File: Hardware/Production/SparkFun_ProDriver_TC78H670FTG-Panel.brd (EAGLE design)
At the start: 50.8 x 57.1 mm, 137 parts, among them J2 LATCH, J3 PTH, J4 LATCH, J5 LATCH, J6 PTH, J7 LATCH, J8 PTH, U1 TC78H670FTG, U2 LM1117

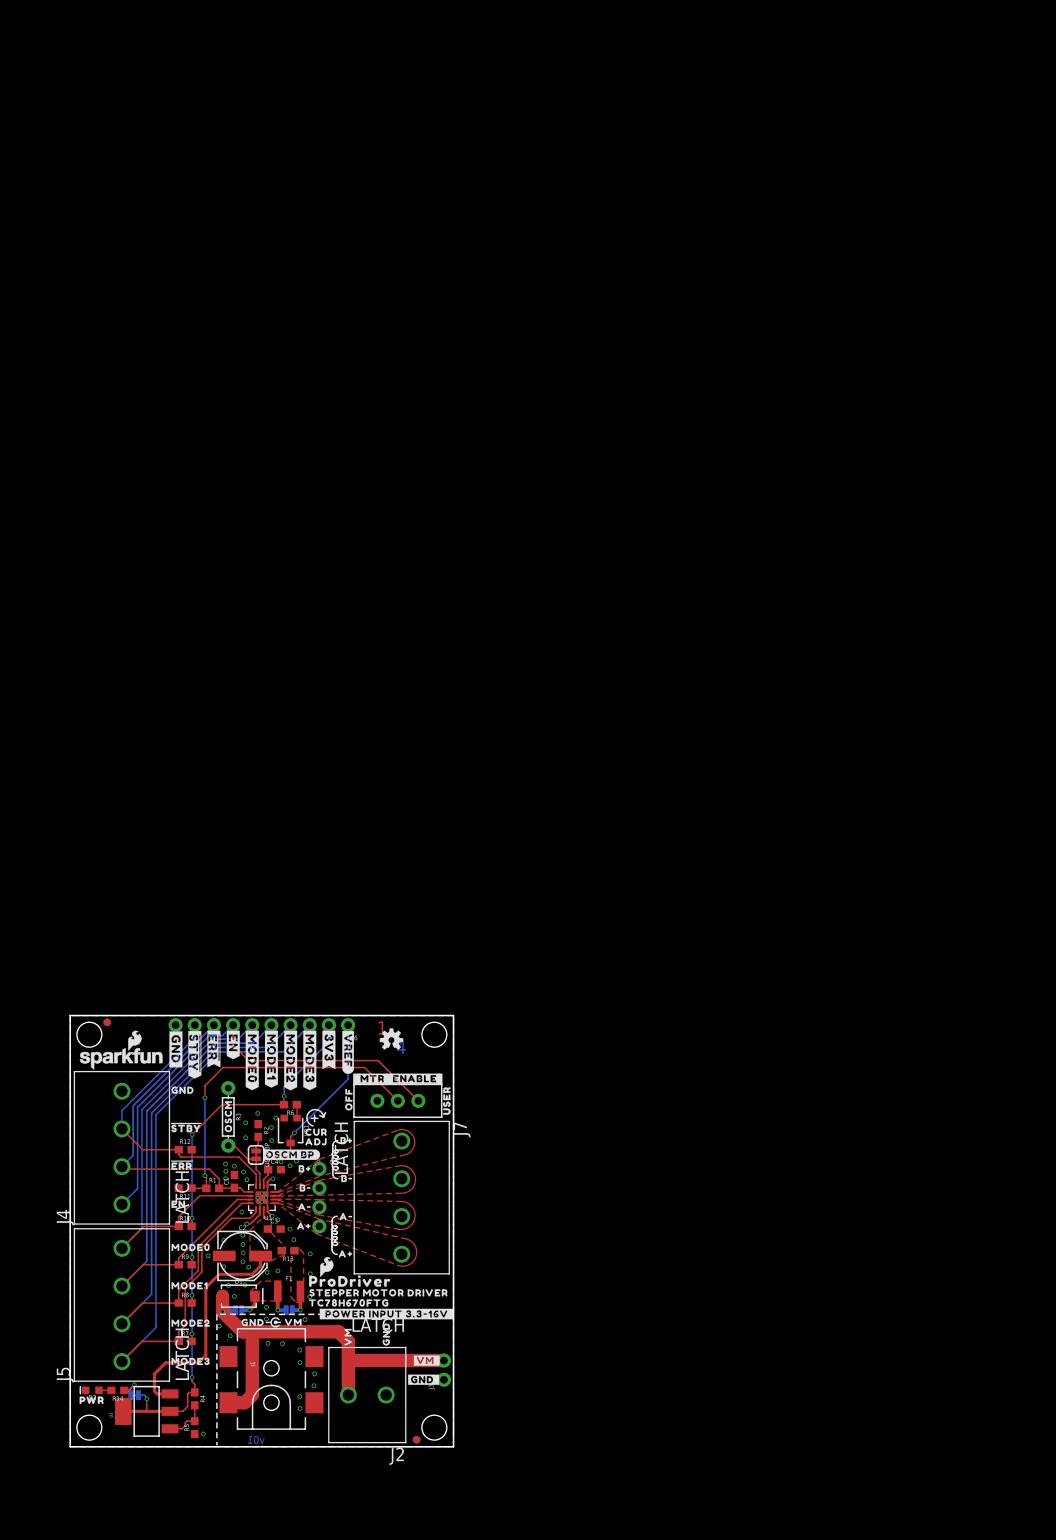
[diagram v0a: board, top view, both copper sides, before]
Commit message: production files - also decided to go with 1 OZ copper
-panelized for proto panel order 2x2
-removed "2OZ Copper" note from special ordering instructions. Fab house for protos (JLC) has huge price jump for 2 OZ, so gonna try 1 OZ for protos and see how heat sinking does.
-adjusted ordering instrutions text file to reflext black soldermask
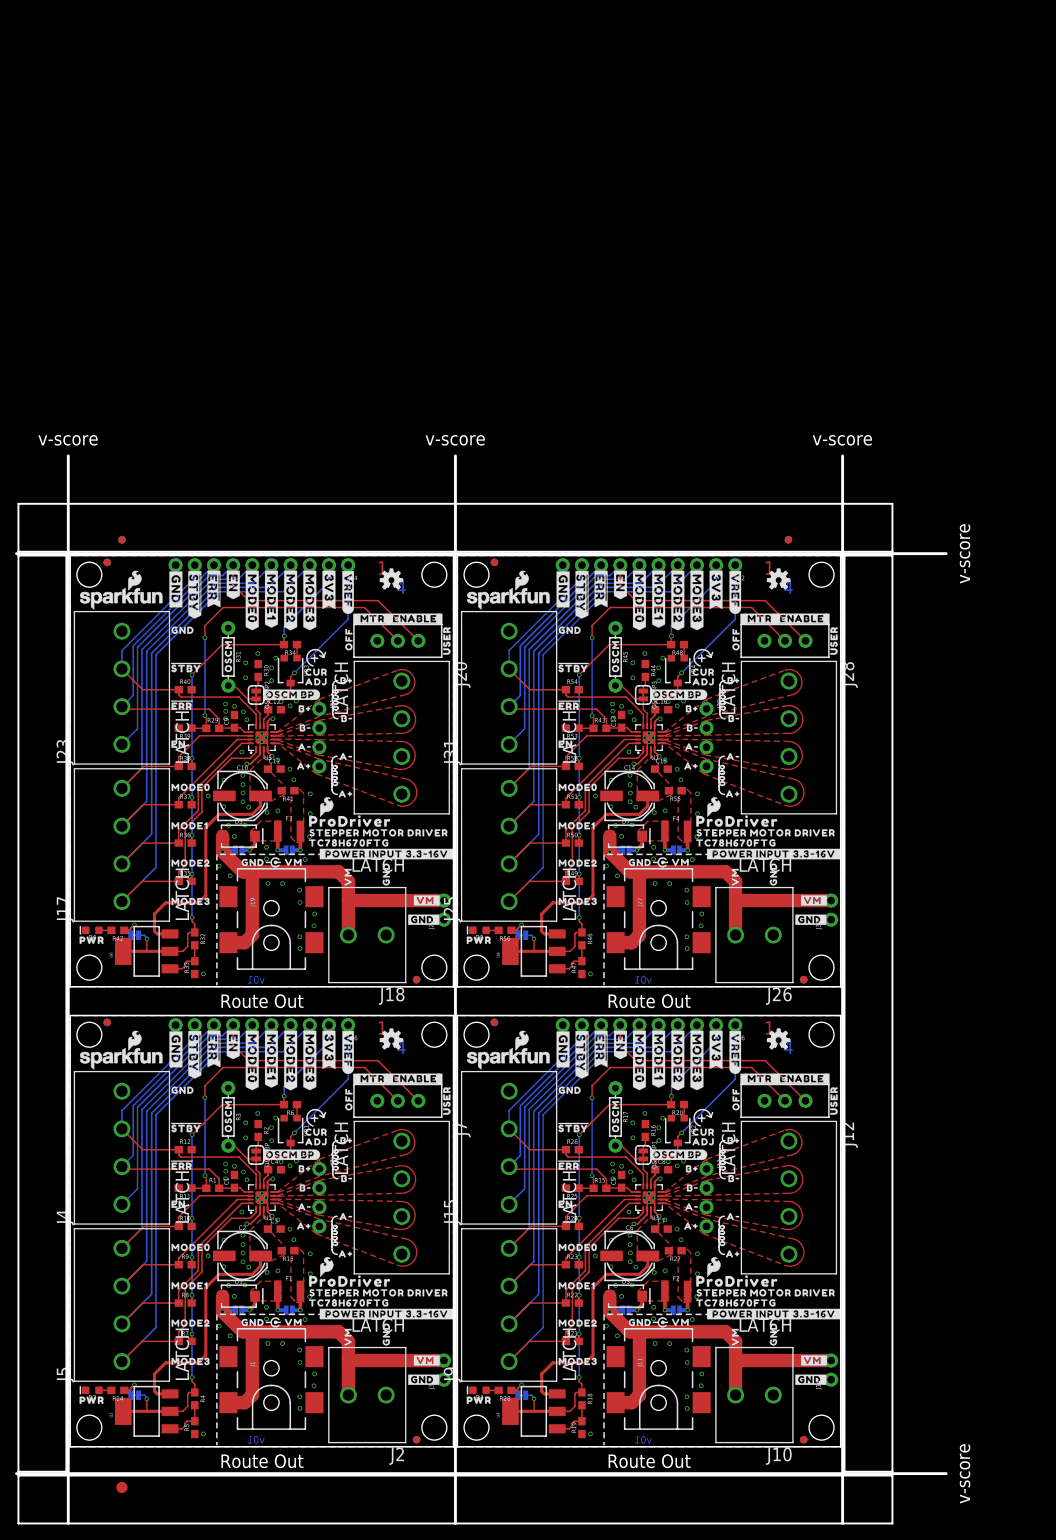
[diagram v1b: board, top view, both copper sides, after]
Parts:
- removed FRAME1: FRAME-LETTER, SparkFun-Aesthetics:CREATIVE_COMMONS
- added C10, C14, C6: 47uF, SparkFun-Capacitors:PANASONIC_D
- added C11, C12, C15, C16, C7, C8: 0.1uF, SparkFun-Capacitors:0603
- added C13, C5, C9: 22nF, SparkFun-Capacitors:0603
- added D1BP1, D1BP2, D1BP3, PTCBP1, PTCBP2, PTCBP3: (no value), SparkFun-Jumpers:SMT-JUMPER_2_NO_SILK
- added D3, D5, D7: 3A/40V/500mV, SparkFun-DiscreteSemi:SMA-DIODE
- added D4, D6, D8: RED, SparkFun-LED:LED-0603
- added E$1, E$2, E$3, E$4: (no value), SparkFun-Aesthetics:FIDUCIAL-1X2
- added E$5: (no value), SparkFun-Retired:FIDUCIAL-1.5X3
- added F2, F3, F4: 16V/1.1A(2.2A TRIP), TC78H670FTG:1210
- added FID10, FID11, FID12, FID13, FID14, FID15, FID16, FID5, FID6, FID7, FID8, FID9: FIDUCIAL1X2, SparkFun-Aesthetics:FIDUCIAL-1X2
- added J10, J18, J26: LATCH, SparkFun-Connectors:LATCHTERMINAL-5MM-2
- added J11, J19, J27: (no value), SparkFun-Connectors:POWER_JACK_SMD_OVERPASTE_TOE
- added J12, J15, J17, J20, J23, J25, J28, J31, J9: LATCH, SparkFun-Connectors:LATCHTERMINAL-5MM-4
- added J13, J21, J29: PTH, SparkFun-Connectors:1X04_NO_SILK
- added J14, J22, J30: PTH, SparkFun-Connectors:1X02_NO_SILK
- added J16, J24, J32: PTH, SparkFun-Connectors:1X10_NO_SILK
- added JP1, JP2, JP3: LED, SparkFun-Jumpers:SMT-JUMPER_2_NC_TRACE_SILK
- added LOGO10, LOGO14, LOGO4: OSHW-LOGOS, SparkFun-Aesthetics:OSHW-LOGO-S
- added LOGO11, LOGO13, LOGO15, LOGO7, LOGO9: SFE_LOGO_NAME_FLAME.1_INCH, SparkFun-Aesthetics:SFE_LOGO_NAME_FLAME_.1
- added LOGO12, LOGO16, LOGO8: SFE_LOGO_FLAME.1_INCH, SparkFun-Aesthetics:SFE_LOGO_FLAME_.1
- added OSCMBP1, OSCMBP2, OSCMBP3: (no value), SparkFun-Jumpers:SMT-JUMPER_2_NC_TRACE_SILK
- added R15, R29, R43: 10k, SparkFun-Resistors:0603
- added R16, R30, R44: 47k, SparkFun-Resistors:0603
- added R17, R31, R45: DNP, SparkFun-Resistors:AXIAL-0.3
- added R18, R32, R46: 240, SparkFun-Resistors:0603
- added R19, R33, R47: 390, SparkFun-Resistors:0603
- added R20, R34, R48: 8.2k, SparkFun-Resistors:0603
- added R21, R22, R23, R24, R25, R26, R35, R36, R37, R38, R39, R40, R49, R50, R51, R52, R53, R54: 22k, SparkFun-Resistors:0603
- added R27, R41, R55: 0, SparkFun-Resistors:0603
- added R28, R42, R56: 1k, SparkFun-Resistors:0603
- added S2, S3, S4: (no value), SparkFun-Switches:SWITCH_SPDT_PTH_11.6X4.0MM_LOCK
- added STANDOFF10, STANDOFF11, STANDOFF12, STANDOFF13, STANDOFF14, STANDOFF15, STANDOFF16, STANDOFF5, STANDOFF6, STANDOFF7, STANDOFF8, STANDOFF9: STAND-OFF, SparkFun-Electromechanical:STAND-OFF
- added U$100, U$186, U$272: (no value), output:MODE10
- added U$101, U$187, U$273: (no value), output:MODE20
- added U$102, U$188, U$274: (no value), output:MODE00
- added U$103, U$189, U$275: (no value), output:#GND_#0
- added U$104, U$190, U$276: (no value), output:#VM_#0
- added U$105, U$177, U$179, U$191, U$263, U$265, U$277, U$91, U$93: (no value), output:GND6
- added U$106, U$178, U$192, U$264, U$278, U$92: (no value), output:VM10
- added U$107, U$159, U$193, U$245, U$279, U$331: (no value), output:TC78H670FTG0
- added U$108, U$160, U$194, U$246, U$280, U$332: (no value), output:STEPPER_MOTOR_DRIVER0
- added U$109, U$144, U$147, U$195, U$230, U$233, U$281, U$316, U$319: (no value), output:#GND#0
- added U$110, U$161, U$196, U$247, U$282, U$333: (no value), output:PRODRIVER0
- added U$111, U$197, U$283: (no value), output:#MTR#0
- added U$112, U$198, U$284: (no value), output:#ENABLE#0
- added U$113, U$174, U$199, U$260, U$285, U$71: (no value), output:B#1
- added U$114, U$173, U$200, U$259, U$286, U$41: (no value), output:B#0
- added U$115, U$176, U$201, U$262, U$287, U$90: (no value), output:A#3
- added U$116, U$175, U$202, U$261, U$288, U$74: (no value), output:A#2
- added U$117, U$203, U$289: (no value), output:EN0
- added U$118, U$204, U$290: (no value), output:#EN#2
- added U$119, U$149, U$205, U$235, U$291, U$321: (no value), output:#MODE0#4
- added U$120, U$150, U$206, U$236, U$292, U$322: (no value), output:#MODE1#4
- added U$121, U$151, U$207, U$237, U$293, U$323: (no value), output:#MODE2#4
- added U$122, U$152, U$208, U$238, U$294, U$324: (no value), output:#MODE3#4
- added U$123, U$153, U$209, U$239, U$295, U$325: (no value), output:#3V3#4
- added U$124, U$154, U$210, U$240, U$296, U$326: (no value), output:#VREF#0
- added U$125, U$211, U$297: (no value), output:#D1_BP#0
- added U$126, U$132, U$212, U$218, U$298, U$304: (no value), output:#B##0
- added U$127, U$133, U$213, U$219, U$299, U$305: (no value), output:#B##1
- added U$128, U$134, U$214, U$220, U$300, U$306: (no value), output:#A##2
- added U$129, U$135, U$215, U$221, U$301, U$307: (no value), output:#A##3
- added U$130, U$145, U$216, U$231, U$302, U$317: (no value), output:#GND#5
- added U$131, U$217, U$303: (no value), output:#_EN_#0
- added U$136, U$222, U$308: (no value), output:#MODE0#0
- added U$137, U$223, U$309: (no value), output:#MODE1#0
- added U$138, U$224, U$310: (no value), output:#MODE2#0
- added U$139, U$225, U$311: (no value), output:#MODE3#0
- added U$140, U$226, U$312: (no value), output:#CLK#S_CLK#0
- added U$141, U$227, U$313: (no value), output:#SET_EN#LATCH#0
- added U$142, U$228, U$314: (no value), output:#UP#DW#S_DATA#0
- added U$143, U$146, U$229, U$232, U$315, U$318: (no value), output:#VM#0
- added U$148, U$234, U$320: (no value), output:#EN#4
- added U$155, U$241, U$327: (no value), output:#CW#CCW#0
- added U$156, U$242, U$328: (no value), output:#PTC_BP#0
- added U$157, U$243, U$329: (no value), output:#LED#0
- added U$158, U$244, U$330: (no value), output:PWR0
- added U$162, U$248, U$334: (no value), output:##STBY##0
- added U$163, U$164, U$249, U$250, U$335, U$336: (no value), output:##STBY##1
- added U$165, U$251, U$337: (no value), output:#STBY#2
- added U$166, U$252, U$338: (no value), output:#ERR#3
- added U$167, U$253, U$339: (no value), output:##ERR##5
- added U$168, U$169, U$254, U$255, U$340, U$341: (no value), output:##ERR##6
- added U$170, U$256, U$342: (no value), output:USER0
- added U$171, U$257, U$343: (no value), output:#OSCM_BP#0
- added U$172, U$258, U$344: (no value), output:#_POWER_INPUT_3#3#16V_#0
- added U$180, U$266, U$94: (no value), output:OFF0
- added U$181, U$267, U$95: (no value), output:OSCM0
- added U$182, U$268, U$96: (no value), output:CUR0
- added U$183, U$269, U$97: (no value), output:ADJ0
- added U$184, U$270, U$98: (no value), TC78H670FTG:CURRENT_ADJUST
- added U$185, U$271, U$99: (no value), output:MODE30
- added U3, U5, U7: TC78H670FTG, TC78H670FTG:P-VQFN16-0303-0.50-001
- added U4, U6, U8: LM1117, SparkFun-IC-Power:SOT223
- added VR2, VR3, VR4: 10k, SparkFun-Resistors:TRIMPOT-SMD-3MM-CLOSED
- LOGO3: value SPECIAL_INSTRUCTIONS-ORDERING -> SFE_LOGO_NAME_FLAME.1_INCH; device SparkFun-Aesthetics:ORDERING_INSTRUCTIONS -> SparkFun-Aesthetics:SFE_LOGO_NAME_FLAME_.1
- moved LOGO3 106.6 mm to (58.1, 51.4)
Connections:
- new net !ERR1: C5.1, J15.2, J16.8, R15.2, U3.13
- new net !ERR2: C9.1, J23.2, J24.8, R29.2, U5.13
- new net !ERR3: C13.1, J31.2, J32.8, R43.2, U7.13
- new net !STBY1: J15.3, J16.9, R26.1, U3.12
- new net !STBY2: J23.3, J24.9, R40.1, U5.12
- new net !STBY3: J31.3, J32.9, R54.1, U7.12
- new net 3.3V1: J16.2, JP1.2, R18.1, R20.2, R21.2, R22.2, R23.2, R24.2, U4.2, U4.4
- new net 3.3V2: J24.2, JP2.2, R32.1, R34.2, R35.2, R36.2, R37.2, R38.2, U6.2, U6.4
- new net 3.3V3: J32.2, JP3.2, R46.1, R48.2, R49.2, R50.2, R51.2, R52.2, U8.2, U8.4
- new net EN1: J15.1, J16.7, S2.1
- new net EN2: J23.1, J24.7, S3.1
- new net EN3: J31.1, J32.7, S4.1
- new net GND1: C5.2, C6.-, C7.2, C8.2, D4.C, J10.1, J11.GND, J11.P$4, J14.1, J15.4, J16.10, R16.1, R17.P$1, R19.1, R25.2, R26.2, U3.17, U3.2, U3.4, U3.9, VR2.3
- new net GND2: C10.-, C11.2, C12.2, C9.2, D6.C, J18.1, J19.GND, J19.P$4, J22.1, J23.4, J24.10, R30.1, R31.P$1, R33.1, R39.2, R40.2, U5.17, U5.2, U5.4, U5.9, VR3.3
- new net GND3: C13.2, C14.-, C15.2, C16.2, D8.C, J26.1, J27.GND, J27.P$4, J30.1, J31.4, J32.10, R44.1, R45.P$1, R47.1, R53.2, R54.2, U7.17, U7.2, U7.4, U7.9, VR4.3
- new net MODE10: J17.3, J24.5, R37.1, U5.15
- new net MODE11: J17.4, J24.6, R38.1, U5.14
- new net MODE12: J25.1, J32.3, R49.1, U7.1
- new net MODE13: J25.2, J32.4, R50.1, U7.16
- new net MODE14: J25.3, J32.5, R51.1, U7.15
- new net MODE15: J25.4, J32.6, R52.1, U7.14
- new net MODE4: J16.3, J9.1, R21.1, U3.1
- new net MODE5: J16.4, J9.2, R22.1, U3.16
- new net MODE6: J16.5, J9.3, R23.1, U3.15
- new net MODE7: J16.6, J9.4, R24.1, U3.14
- new net MODE8: J17.1, J24.3, R35.1, U5.1
- new net MODE9: J17.2, J24.4, R36.1, U5.16
- new net N$10: OSCMBP1.1, R16.2
- new net N$11: R18.2, R19.2, U4.1
- new net N$13: R20.1, VR2.1
- new net N$14: D1BP1.2, D3.C, F2.1, PTCBP1.1
- new net N$15: F2.2, PTCBP1.2, R27.1
- new net N$16: D4.A, R28.2
- new net N$17: JP1.1, R28.1
- new net N$18: R15.1, R25.1, S2.2
- new net N$21: OSCMBP2.1, R30.2
- new net N$22: R32.2, R33.2, U6.1
- new net N$23: R34.1, VR3.1
- new net N$24: D1BP2.2, D5.C, F3.1, PTCBP2.1
- new net N$25: F3.2, PTCBP2.2, R41.1
- new net N$26: D6.A, R42.2
- new net N$27: JP2.1, R42.1
- new net N$28: R29.1, R39.1, S3.2
- new net N$31: OSCMBP3.1, R44.2
- new net N$32: R46.2, R47.2, U8.1
- new net N$33: R48.1, VR4.1
- new net N$34: D1BP3.2, D7.C, F4.1, PTCBP3.1
- new net N$35: F4.2, PTCBP3.2, R55.1
- new net N$36: D8.A, R56.2
- new net N$37: JP3.1, R56.1
- new net N$38: R43.1, R53.1, S4.2
- new net OSCM1: OSCMBP1.2, R17.P$2, U3.11
- new net OSCM2: OSCMBP2.2, R31.P$2, U5.11
- new net OSCM3: OSCMBP3.2, R45.P$2, U7.11
- new net OUT_A+1: J12.4, J13.4, U3.5
- new net OUT_A+2: J20.4, J21.4, U5.5
- new net OUT_A+3: J28.4, J29.4, U7.5
- new net OUT_A-1: J12.3, J13.3, U3.6
- new net OUT_A-2: J20.3, J21.3, U5.6
- new net OUT_A-3: J28.3, J29.3, U7.6
- new net OUT_B+1: J12.1, J13.1, U3.8
- new net OUT_B+2: J20.1, J21.1, U5.8
- new net OUT_B+3: J28.1, J29.1, U7.8
- new net OUT_B-1: J12.2, J13.2, U3.7
- new net OUT_B-2: J20.2, J21.2, U5.7
- new net OUT_B-3: J28.2, J29.2, U7.7
- new net RAW1: D1BP1.1, D3.A, J10.2, J11.VIN0, J14.2
- new net RAW2: D1BP2.1, D5.A, J18.2, J19.VIN0, J22.2
- new net RAW3: D1BP3.1, D7.A, J26.2, J27.VIN0, J30.2
- new net VM1: C6.+, C7.1, R27.2, U3.3, U4.3
- new net VM2: C10.+, C11.1, R41.2, U5.3, U6.3
- new net VM3: C14.+, C15.1, R55.2, U7.3, U8.3
- new net VREF1: C8.1, J16.1, U3.10, VR2.2
- new net VREF2: C12.1, J24.1, U5.10, VR3.2
- new net VREF3: C16.1, J32.1, U7.10, VR4.2
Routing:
- net MODE12: track 0.00 -> 91.8 mm
- net MODE4: track 0.00 -> 91.8 mm
- net MODE8: track 0.00 -> 91.8 mm
- net 3.3V3: track 0.00 -> 79.8 mm, vias 0 -> 8
- net 3.3V1: track 0.00 -> 79.8 mm, vias 0 -> 8
- net 3.3V2: track 0.00 -> 79.8 mm, vias 0 -> 8
- net MODE5: track 0.00 -> 79.3 mm
- net MODE13: track 0.00 -> 79.3 mm
- net MODE9: track 0.00 -> 79.3 mm
- net MODE6: track 0.00 -> 68.1 mm
- net MODE14: track 0.00 -> 68.1 mm
- net MODE10: track 0.00 -> 68.1 mm
- net EN3: track 0.00 -> 61.1 mm
- net EN2: track 0.00 -> 61.1 mm
- net EN1: track 0.00 -> 61.1 mm
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- added copper zone on layer 1, net GND1
- added copper zone on layer 15, net GND1
- added copper zone on layer 16, net GND1
- added copper zone on layer 2, net GND1
- added copper zone on layer 1, net GND2
- added copper zone on layer 15, net GND2
- added copper zone on layer 16, net GND2
- added copper zone on layer 2, net GND2
- added copper zone on layer 1, net GND3
- added copper zone on layer 15, net GND3
- added copper zone on layer 16, net GND3
- added copper zone on layer 2, net GND3
- added copper zone on layer 1, net N$14
- added copper zone on layer 1, net N$15
- added copper zone on layer 1, net N$24
- added copper zone on layer 1, net N$25
- added copper zone on layer 1, net N$34
- added copper zone on layer 1, net N$35
- added copper zone on layer 1, net OUT_A+1
- added copper zone on layer 1, net OUT_A+2
- added copper zone on layer 1, net OUT_A+3
- added copper zone on layer 1, net OUT_A-1
- added copper zone on layer 1, net OUT_A-2
- added copper zone on layer 1, net OUT_A-3
- added copper zone on layer 1, net OUT_B+1
- added copper zone on layer 1, net OUT_B+2
- added copper zone on layer 1, net OUT_B+3
- added copper zone on layer 1, net OUT_B-1
- added copper zone on layer 1, net OUT_B-2
- added copper zone on layer 1, net OUT_B-3
- added copper zone on layer 1, net VM1
- added copper zone on layer 1, net VM2
- added copper zone on layer 1, net VM3
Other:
- board size 50.8 x 57.1 mm -> 123.2 x 141.5 mm
- board text added: "Route Out"
- board text added: "v-score"
- board text removed: "4-Layer Board"
- board text removed: "LAYER NUMBERS"
- board text removed: "Pete Lewis"
- board text removed: "Selective Solder Nozzle Width: 0.354""
- board text removed: "This is a 4-LAYER board!"

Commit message: Production files for v10
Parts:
- added C17, C21: 22nF, SparkFun-Capacitors:0603
- added C18, C22: 47uF, SparkFun-Capacitors:PANASONIC_D
- added C19, C20, C23, C24: 0.1uF, SparkFun-Capacitors:0603
- added D10, D12: RED, SparkFun-LED:LED-0603
- added D11, D9: 3A/40V/500mV, SparkFun-DiscreteSemi:SMA-DIODE
- added D1BP4, D1BP5, PTCBP4, PTCBP5: (no value), SparkFun-Jumpers:SMT-JUMPER_2_NO_SILK
- added F5, F6: 16V/1.1A(2.2A TRIP), TC78H670FTG:1210
- added FID17, FID18, FID19, FID20, FID21, FID22, FID23, FID24: FIDUCIAL1X2, SparkFun-Aesthetics:FIDUCIAL-1X2
- added J33, J36, J39, J41, J44, J47: LATCH, SparkFun-Connectors:LATCHTERMINAL-5MM-4
- added J34, J42: LATCH, SparkFun-Connectors:LATCHTERMINAL-5MM-2
- added J35, J43: (no value), SparkFun-Connectors:POWER_JACK_SMD_OVERPASTE_TOE
- added J37, J45: PTH, SparkFun-Connectors:1X04_NO_SILK
- added J38, J46: PTH, SparkFun-Connectors:1X02_NO_SILK
- added J40, J48: PTH, SparkFun-Connectors:1X10_NO_SILK
- added JP5, JP6: LED, SparkFun-Jumpers:SMT-JUMPER_2_NC_TRACE_SILK
- added LOGO17, LOGO21: SFE_LOGO_NAME_FLAME.1_INCH, SparkFun-Aesthetics:SFE_LOGO_NAME_FLAME_.1
- added LOGO18, LOGO22: OSHW-LOGOS, SparkFun-Aesthetics:OSHW-LOGO-S
- added LOGO19, LOGO23: SFE_LOGO_NAME_FLAME.1_INCH, SparkFun-Aesthetics:SFE_LOGO_FLAME_.1
- added LOGO20, LOGO24: SFE_LOGO_FLAME.1_INCH, SparkFun-Aesthetics:SFE_LOGO_FLAME_.1
- added OSCMBP4, OSCMBP5: (no value), SparkFun-Jumpers:SMT-JUMPER_2_NC_TRACE_SILK
- added R57, R71: 10k, SparkFun-Resistors:0603
- added R58, R72: 47k, SparkFun-Resistors:0603
- added R59, R73: DNP, SparkFun-Resistors:AXIAL-0.3
- added R60, R74: 240, SparkFun-Resistors:0603
- added R61, R75: 390, SparkFun-Resistors:0603
- added R62, R76: 8.2k, SparkFun-Resistors:0603
- added R63, R64, R65, R66, R67, R68, R77, R78, R79, R80, R81, R82: 22k, SparkFun-Resistors:0603
- added R69, R83: 0, SparkFun-Resistors:0603
- added R70, R84: 1k, SparkFun-Resistors:0603
- added S5, S6: (no value), SparkFun-Switches:SWITCH_SPDT_PTH_11.6X4.0MM_LOCK
- added STANDOFF17, STANDOFF18, STANDOFF19, STANDOFF20, STANDOFF21, STANDOFF22, STANDOFF23, STANDOFF24: STAND-OFF, SparkFun-Electromechanical:STAND-OFF
- added U$345, U$433, U$521: (no value), output:##STBY##7
- added U$346, U$434, U$522: (no value), output:#GND#8
- added U$347, U$435, U$523: (no value), output:#PTC_BP#9
- added U$348, U$436, U$524: (no value), output:#D1_BP#10
- added U$349, U$437, U$525: (no value), output:#LED#10
- added U$350, U$438, U$526: (no value), output2:#3V3#4
- added U$351, U$439, U$527: (no value), output2:##ERR##5
- added U$352, U$440, U$528: (no value), output:#_POWER_INPUT_3#6#16V_#0
- added U$353, U$380, U$441, U$468: (no value), output:B#0
- added U$354, U$379, U$442, U$467: (no value), output:B#1
- added U$355, U$382, U$443, U$470: (no value), output:A#2
- added U$356, U$381, U$444, U$469: (no value), output:A#3
- added U$357, U$359, U$371, U$445, U$447, U$459: (no value), output:GND6
- added U$358, U$372, U$446, U$460: (no value), output:VM10
- added U$360, U$448: (no value), output:OFF0
- added U$361, U$449: (no value), output:OSCM0
- added U$362, U$450: (no value), output:CUR0
- added U$363, U$451: (no value), output:ADJ0
- added U$364, U$452: (no value), TC78H670FTG:CURRENT_ADJUST
- added U$365, U$453: (no value), output:MODE30
- added U$366, U$454: (no value), output:MODE10
- added U$367, U$455: (no value), output:MODE20
- added U$368, U$456: (no value), output:MODE00
- added U$369, U$457: (no value), output:#GND_#0
- added U$370, U$458: (no value), output:#VM_#0
- added U$373, U$413, U$461, U$501: (no value), output:TC78H670FTG0
- added U$374, U$414, U$462, U$502: (no value), output:STEPPER_MOTOR_DRIVER0
- added U$375, U$408, U$410, U$463, U$496, U$498: (no value), output:#GND#0
- added U$376, U$415, U$464, U$503: (no value), output:PRODRIVER0
- added U$377, U$465: (no value), output:#MTR#0
- added U$378, U$466: (no value), output:#ENABLE#0
- added U$383, U$471: (no value), output:EN0
- added U$384, U$472: (no value), output:#EN#2
- added U$385, U$473: (no value), output:#MODE0#4
- added U$386, U$474: (no value), output:#MODE1#4
- added U$387, U$475: (no value), output:#MODE2#4
- added U$388, U$476: (no value), output:#MODE3#4
- added U$389, U$477: (no value), output:#VREF#0
- added U$390, U$396, U$478, U$484: (no value), output:#B##0
- added U$391, U$397, U$479, U$485: (no value), output:#B##1
- added U$392, U$398, U$480, U$486: (no value), output:#A##2
- added U$393, U$399, U$481, U$487: (no value), output:#A##3
- added U$394, U$482: (no value), output:#GND#5
- added U$395, U$483: (no value), output:#_EN_#0
- added U$400, U$488: (no value), output:#MODE0#0
- added U$401, U$489: (no value), output:#MODE1#0
- added U$402, U$490: (no value), output:#MODE2#0
- added U$403, U$491: (no value), output:#MODE3#0
- added U$404, U$492: (no value), output:#CLK#S_CLK#0
- added U$405, U$493: (no value), output:#SET_EN#LATCH#0
- added U$406, U$494: (no value), output:#UP#DW#S_DATA#0
- added U$407, U$409, U$495, U$497: (no value), output:#VM#0
- added U$411, U$499: (no value), output:#CW#CCW#0
- added U$412, U$500: (no value), output:PWR0
- added U$416, U$504: (no value), output:##STBY##0
- added U$417, U$505: (no value), output:##STBY##1
- added U$418, U$506: (no value), output:#STBY#2
- added U$419, U$507: (no value), output:#ERR#3
- added U$420, U$508: (no value), output:##ERR##5
- added U$421, U$509: (no value), output:USER0
- added U$422, U$510: (no value), output:#OSCM_BP#0
- added U$423, U$511: PRODRIVER_LOGO, TC78H670FTG:PRODRIVER_LOGO
- added U$424, U$512: (no value), SparkFun-Aesthetics:OSHW-LOGO-S
- added U$425, U$513: (no value), output:#MODE0#1
- added U$426, U$514: (no value), output:#MODE1#1
- added U$427, U$515: (no value), output:#MODE2#2
- added U$428, U$516: (no value), output:#MODE3#3
- added U$429, U$517: (no value), output:#3V3#4
- added U$430, U$518: (no value), output:#VREF#4
- added U$431, U$519: (no value), output:#EN#5
- added U$432, U$520: (no value), output:##ERR##6
- added U10, U12: LM1117, SparkFun-IC-Power:SOT223
- added U11, U9: TC78H670FTG, TC78H670FTG:P-VQFN16-0303-0.50-001
- added VR5, VR6: 10k, SparkFun-Resistors:TRIMPOT-SMD-3MM-CLOSED
- LOGO11, LOGO15, LOGO5, LOGO7: device SparkFun-Aesthetics:SFE_LOGO_NAME_FLAME_.1 -> SparkFun-Aesthetics:SFE_LOGO_FLAME_.1
- U$100: device output:MODE10 -> TC78H670FTG:CURRENT_ADJUST
- U$101: device output:MODE20 -> output:MODE30
- U$102: device output:MODE00 -> output:MODE10
- U$103: device output:#GND_#0 -> output:MODE20
- U$104: device output:#VM_#0 -> output:MODE00
- U$105: device output:GND6 -> output:#GND_#0
- U$106: device output:VM10 -> output:#VM_#0
- U$107: device output:TC78H670FTG0 -> output:GND6
- U$108: device output:STEPPER_MOTOR_DRIVER0 -> output:VM10
- U$109: device output:#GND#0 -> output:TC78H670FTG0
- U$110: device output:PRODRIVER0 -> output:STEPPER_MOTOR_DRIVER0
- U$111: device output:#MTR#0 -> output:#GND#0
- U$112: device output:#ENABLE#0 -> output:PRODRIVER0
- U$113: device output:B#1 -> output:#MTR#0
- U$114: device output:B#0 -> output:#ENABLE#0
- U$115: device output:A#3 -> output:B#1
- U$116: device output:A#2 -> output:B#0
- U$117: device output:EN0 -> output:A#3
- U$118: device output:#EN#2 -> output:A#2
- U$119: device output:#MODE0#4 -> output:EN0
- U$120: device output:#MODE1#4 -> output:#EN#2
- U$121: device output:#MODE2#4 -> output:#MODE0#4
- U$122: device output:#MODE3#4 -> output:#MODE1#4
- U$123: device output:#3V3#4 -> output:#MODE2#4
- U$124: device output:#VREF#0 -> output:#MODE3#4
- U$125: device output:#D1_BP#0 -> output:#VREF#0
- U$145, U$231: device output:#GND#5 -> output:#VM#0
- U$146, U$232: device output:#VM#0 -> output:#GND#0
- U$147: device output:#GND#0 -> output:#CW#CCW#0
- U$148: device output:#EN#4 -> output:PWR0
- U$149: device output:#MODE0#4 -> output:TC78H670FTG0
- U$150: device output:#MODE1#4 -> output:STEPPER_MOTOR_DRIVER0
- U$151: device output:#MODE2#4 -> output:PRODRIVER0
- U$152: device output:#MODE3#4 -> output:##STBY##0
- U$153: device output:#3V3#4 -> output:##STBY##1
- U$154: device output:#VREF#0 -> output:#STBY#2
- U$155: device output:#CW#CCW#0 -> output:#ERR#3
- U$156: device output:#PTC_BP#0 -> output:##ERR##5
- U$157: device output:#LED#0 -> output:USER0
- U$158: device output:PWR0 -> output:#OSCM_BP#0
- U$159: value (none) -> PRODRIVER_LOGO; device output:TC78H670FTG0 -> TC78H670FTG:PRODRIVER_LOGO
- U$160: device output:STEPPER_MOTOR_DRIVER0 -> SparkFun-Aesthetics:OSHW-LOGO-S
- U$161: device output:PRODRIVER0 -> output:#MODE0#1
- U$162: device output:##STBY##0 -> output:#MODE1#1
- U$163: device output:##STBY##1 -> output:#MODE2#2
- U$164: device output:##STBY##1 -> output:#MODE3#3
- U$165: device output:#STBY#2 -> output:#3V3#4
- U$166: device output:#ERR#3 -> output:#VREF#4
- U$167: device output:##ERR##5 -> output:#EN#5
- U$169, U$54: device output:##ERR##6 -> output:##STBY##7
- U$170: device output:USER0 -> output:#GND#8
- U$171: device output:#OSCM_BP#0 -> output:#PTC_BP#9
- U$172: device output:#_POWER_INPUT_3#3#16V_#0 -> output:#D1_BP#10
- U$173: device output:B#0 -> output:#LED#10
- U$174: device output:B#1 -> output2:#3V3#4
- U$175: device output:A#2 -> output2:##ERR##5
- U$176: device output:A#3 -> output:#_POWER_INPUT_3#6#16V_#0
- U$177, U$265: device output:GND6 -> output:B#0
- U$178: device output:VM10 -> output:B#1
- U$179: device output:GND6 -> output:A#2
- U$180: device output:OFF0 -> output:A#3
- U$181: device output:OSCM0 -> output:GND6
- U$182: device output:CUR0 -> output:VM10
- U$183, U$269: device output:ADJ0 -> output:GND6
- U$184: device TC78H670FTG:CURRENT_ADJUST -> output:OFF0
- U$185: device output:MODE30 -> output:OSCM0
- U$186: device output:MODE10 -> output:CUR0
- U$187: device output:MODE20 -> output:ADJ0
- U$188: device output:MODE00 -> TC78H670FTG:CURRENT_ADJUST
- U$189: device output:#GND_#0 -> output:MODE30
- U$190: device output:#VM_#0 -> output:MODE10
- U$191: device output:GND6 -> output:MODE20
- U$192: device output:VM10 -> output:MODE00
- U$193: device output:TC78H670FTG0 -> output:#GND_#0
- U$194: device output:STEPPER_MOTOR_DRIVER0 -> output:#VM_#0
- U$195: device output:#GND#0 -> output:GND6
- U$196: device output:PRODRIVER0 -> output:VM10
- U$197: device output:#MTR#0 -> output:TC78H670FTG0
- U$198: device output:#ENABLE#0 -> output:STEPPER_MOTOR_DRIVER0
- U$199: device output:B#1 -> output:#GND#0
- U$200: device output:B#0 -> output:PRODRIVER0
- U$201: device output:A#3 -> output:#MTR#0
- U$202: device output:A#2 -> output:#ENABLE#0
- U$203: device output:EN0 -> output:B#1
- U$204: device output:#EN#2 -> output:B#0
- U$205: device output:#MODE0#4 -> output:A#3
- U$206: device output:#MODE1#4 -> output:A#2
- U$207: device output:#MODE2#4 -> output:EN0
- U$208: device output:#MODE3#4 -> output:#EN#2
- U$209: device output:#3V3#4 -> output:#MODE0#4
- U$210: device output:#VREF#0 -> output:#MODE1#4
- U$211: device output:#D1_BP#0 -> output:#MODE2#4
- U$212: device output:#B##0 -> output:#MODE3#4
- U$213: device output:#B##1 -> output:#VREF#0
- U$214, U$220: device output:#A##2 -> output:#B##0
- U$215, U$221: device output:#A##3 -> output:#B##1
- U$216: device output:#GND#5 -> output:#A##2
- U$217: device output:#_EN_#0 -> output:#A##3
- U$218: device output:#B##0 -> output:#GND#5
- U$219: device output:#B##1 -> output:#_EN_#0
- U$222: device output:#MODE0#0 -> output:#A##2
- U$223: device output:#MODE1#0 -> output:#A##3
- U$224: device output:#MODE2#0 -> output:#MODE0#0
- U$225: device output:#MODE3#0 -> output:#MODE1#0
- U$226: device output:#CLK#S_CLK#0 -> output:#MODE2#0
- U$227: device output:#SET_EN#LATCH#0 -> output:#MODE3#0
- U$228: device output:#UP#DW#S_DATA#0 -> output:#CLK#S_CLK#0
- U$229: device output:#VM#0 -> output:#SET_EN#LATCH#0
- U$230: device output:#GND#0 -> output:#UP#DW#S_DATA#0
- U$233, U$319: device output:#GND#0 -> output:#VM#0
- U$234, U$320: device output:#EN#4 -> output:#GND#0
- U$235: device output:#MODE0#4 -> output:#CW#CCW#0
- U$236: device output:#MODE1#4 -> output:PWR0
- U$237: device output:#MODE2#4 -> output:TC78H670FTG0
- U$238: device output:#MODE3#4 -> output:STEPPER_MOTOR_DRIVER0
- U$239: device output:#3V3#4 -> output:PRODRIVER0
- U$240: device output:#VREF#0 -> output:##STBY##0
- U$241: device output:#CW#CCW#0 -> output:##STBY##1
- U$242: device output:#PTC_BP#0 -> output:#STBY#2
- U$243: device output:#LED#0 -> output:#ERR#3
- U$244: device output:PWR0 -> output:##ERR##5
- U$245: device output:TC78H670FTG0 -> output:USER0
- U$246: device output:STEPPER_MOTOR_DRIVER0 -> output:#OSCM_BP#0
- U$247: value (none) -> PRODRIVER_LOGO; device output:PRODRIVER0 -> TC78H670FTG:PRODRIVER_LOGO
- U$248: device output:##STBY##0 -> SparkFun-Aesthetics:OSHW-LOGO-S
- U$249: device output:##STBY##1 -> output:#MODE0#1
- U$250: device output:##STBY##1 -> output:#MODE1#1
- U$251: device output:#STBY#2 -> output:#MODE2#2
- U$252: device output:#ERR#3 -> output:#MODE3#3
- U$253: device output:##ERR##5 -> output:#3V3#4
- U$254: device output:##ERR##6 -> output:#VREF#4
- U$255: device output:##ERR##6 -> output:#EN#5
- U$256: device output:USER0 -> output:##ERR##6
- U$257: device output:#OSCM_BP#0 -> output:##STBY##7
- U$258: device output:#_POWER_INPUT_3#3#16V_#0 -> output:#GND#8
- U$259: device output:B#0 -> output:#PTC_BP#9
- U$260: device output:B#1 -> output:#D1_BP#10
- U$261: device output:A#2 -> output:#LED#10
- U$262: device output:A#3 -> output2:#3V3#4
- U$263: device output:GND6 -> output2:##ERR##5
- U$264: device output:VM10 -> output:#_POWER_INPUT_3#6#16V_#0
- U$266: device output:OFF0 -> output:B#1
- U$267: device output:OSCM0 -> output:A#2
- U$268: device output:CUR0 -> output:A#3
- U$270: device TC78H670FTG:CURRENT_ADJUST -> output:VM10
- U$271: device output:MODE30 -> output:GND6
- U$272: device output:MODE10 -> output:OFF0
- U$273: device output:MODE20 -> output:OSCM0
- U$274: device output:MODE00 -> output:CUR0
- U$275: device output:#GND_#0 -> output:ADJ0
- U$276: device output:#VM_#0 -> TC78H670FTG:CURRENT_ADJUST
- U$277: device output:GND6 -> output:MODE30
- U$278: device output:VM10 -> output:MODE10
- U$279: device output:TC78H670FTG0 -> output:MODE20
- U$280: device output:STEPPER_MOTOR_DRIVER0 -> output:MODE00
- U$281: device output:#GND#0 -> output:#GND_#0
- U$282: device output:PRODRIVER0 -> output:#VM_#0
- U$283: device output:#MTR#0 -> output:GND6
- U$284: device output:#ENABLE#0 -> output:VM10
- U$285: device output:B#1 -> output:TC78H670FTG0
- U$286: device output:B#0 -> output:STEPPER_MOTOR_DRIVER0
- U$287: device output:A#3 -> output:#GND#0
- U$288: device output:A#2 -> output:PRODRIVER0
- U$289: device output:EN0 -> output:#MTR#0
- U$290: device output:#EN#2 -> output:#ENABLE#0
- U$291: device output:#MODE0#4 -> output:B#1
- U$292: device output:#MODE1#4 -> output:B#0
- U$293: device output:#MODE2#4 -> output:A#3
- U$294: device output:#MODE3#4 -> output:A#2
- U$295: device output:#3V3#4 -> output:EN0
- U$296: device output:#VREF#0 -> output:#EN#2
- U$297: device output:#D1_BP#0 -> output:#MODE0#4
- U$298: device output:#B##0 -> output:#MODE1#4
- U$299: device output:#B##1 -> output:#MODE2#4
- U$300: device output:#A##2 -> output:#MODE3#4
- U$301: device output:#A##3 -> output:#VREF#0
- U$302: device output:#GND#5 -> output:#B##0
- U$303: device output:#_EN_#0 -> output:#B##1
- U$304: device output:#B##0 -> output:#A##2
- U$305: device output:#B##1 -> output:#A##3
- U$306: device output:#A##2 -> output:#GND#5
- U$307: device output:#A##3 -> output:#_EN_#0
- U$308: device output:#MODE0#0 -> output:#B##0
- U$309: device output:#MODE1#0 -> output:#B##1
- U$310: device output:#MODE2#0 -> output:#A##2
- U$311: device output:#MODE3#0 -> output:#A##3
- U$312: device output:#CLK#S_CLK#0 -> output:#MODE0#0
- U$313: device output:#SET_EN#LATCH#0 -> output:#MODE1#0
- U$314: device output:#UP#DW#S_DATA#0 -> output:#MODE2#0
- U$315: device output:#VM#0 -> output:#MODE3#0
- U$316: device output:#GND#0 -> output:#CLK#S_CLK#0
- U$317: device output:#GND#5 -> output:#SET_EN#LATCH#0
- U$318: device output:#VM#0 -> output:#UP#DW#S_DATA#0
- U$321: device output:#MODE0#4 -> output:#VM#0
- U$322: device output:#MODE1#4 -> output:#GND#0
- U$323: device output:#MODE2#4 -> output:#CW#CCW#0
- U$324: device output:#MODE3#4 -> output:PWR0
- U$325: device output:#3V3#4 -> output:TC78H670FTG0
- U$326: device output:#VREF#0 -> output:STEPPER_MOTOR_DRIVER0
- U$327: device output:#CW#CCW#0 -> output:PRODRIVER0
- U$328: device output:#PTC_BP#0 -> output:##STBY##0
- U$329: device output:#LED#0 -> output:##STBY##1
- U$330: device output:PWR0 -> output:#STBY#2
- U$331: device output:TC78H670FTG0 -> output:#ERR#3
- U$332: device output:STEPPER_MOTOR_DRIVER0 -> output:##ERR##5
- U$333: device output:PRODRIVER0 -> output:USER0
- U$334: device output:##STBY##0 -> output:#OSCM_BP#0
- U$335: value (none) -> PRODRIVER_LOGO; device output:##STBY##1 -> TC78H670FTG:PRODRIVER_LOGO
- U$336: device output:##STBY##1 -> SparkFun-Aesthetics:OSHW-LOGO-S
- U$337: device output:#STBY#2 -> output:#MODE0#1
- U$338: device output:#ERR#3 -> output:#MODE1#1
- U$339: device output:##ERR##5 -> output:#MODE2#2
- U$340: device output:##ERR##6 -> output:#MODE3#3
- U$341: device output:##ERR##6 -> output:#3V3#4
- U$342: device output:USER0 -> output:#VREF#4
- U$343: device output:#OSCM_BP#0 -> output:#EN#5
- U$344: device output:#_POWER_INPUT_3#3#16V_#0 -> output:##ERR##6
- U$35: device output:#3V3#4 -> output2:##ERR##5
- U$36: device output:##ERR##6 -> output:#_POWER_INPUT_3#6#16V_#0
- U$38: device output:#D1_BP#0 -> output:#LED#10
- U$39: device output:#LED#0 -> output:B#0
- U$41: value (none) -> PRODRIVER_LOGO; device output:B#0 -> TC78H670FTG:PRODRIVER_LOGO
- U$45: device output:#_POWER_INPUT_3#3#16V_#0 -> output:B#1
- U$64: device output:#PTC_BP#0 -> output:#D1_BP#10
- U$70: device output:#GND#5 -> output:#PTC_BP#9
- U$71: device output:B#1 -> SparkFun-Aesthetics:OSHW-LOGO-S
- U$74: device output:A#2 -> output:#MODE0#1
- U$75: device output:#EN#4 -> output2:#3V3#4
- U$76: device output:#MODE0#4 -> output:A#2
- U$77: device output:#MODE1#4 -> output:A#3
- U$78: device output:#MODE2#4 -> output:GND6
- U$79: device output:#MODE3#4 -> output:VM10
- U$80: device output:#3V3#4 -> output:#VREF#4
- U$81: device output:#VREF#0 -> output:GND6
- U$88: device output:##STBY##1 -> output:OFF0
- U$90: device output:A#3 -> output:#MODE1#1
- U$91: device output:GND6 -> output:#MODE2#2
- U$92: device output:VM10 -> output:#MODE3#3
- U$93: device output:GND6 -> output:#3V3#4
- U$94: device output:OFF0 -> output:#EN#5
- U$95: device output:OSCM0 -> output:##ERR##6
- U$96: device output:CUR0 -> output:#GND#8
- U$97: device output:ADJ0 -> output:OSCM0
- U$98: device TC78H670FTG:CURRENT_ADJUST -> output:CUR0
- U$99: device output:MODE30 -> output:ADJ0
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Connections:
- new net !ERR4: C17.1, J39.2, J40.8, R57.2, U9.13
- new net !ERR5: C21.1, J47.2, J48.8, R71.2, U11.13
- new net !STBY4: J39.3, J40.9, R68.1, U9.12
- new net !STBY5: J47.3, J48.9, R82.1, U11.12
- new net 3.3V4: J40.2, JP5.2, R60.1, R62.2, R63.2, R64.2, R65.2, R66.2, U10.2, U10.4
- new net 3.3V5: J48.2, JP6.2, R74.1, R76.2, R77.2, R78.2, R79.2, R80.2, U12.2, U12.4
- new net EN4: J39.1, J40.7, S5.1
- new net EN5: J47.1, J48.7, S6.1
- new net GND4: C17.2, C18.-, C19.2, C20.2, D10.C, J34.1, J35.GND, J35.P$4, J38.1, J39.4, J40.10, R58.1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
- new net GND5: C21.2, C22.-, C23.2, C24.2, D12.C, J42.1, J43.GND, J43.P$4, J46.1, J47.4, J48.10, R72.1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
- new net MODE16: J33.1, J40.3, R63.1, U9.1
- new net MODE17: J33.2, J40.4, R64.1, U9.16
- new net MODE18: J33.3, J40.5, R65.1, U9.15
- new net MODE19: J33.4, J40.6, R66.1, U9.14
- new net MODE20: J41.1, J48.3, R77.1, U11.1
- new net MODE21: J41.2, J48.4, R78.1, U11.16
- new net MODE22: J41.3, J48.5, R79.1, U11.15
- new net MODE23: J41.4, J48.6, R80.1, U11.14
- new net N$41: OSCMBP4.1, R58.2
- new net N$42: R60.2, R61.2, U10.1
- new net N$43: R62.1, VR5.1
- new net N$44: D1BP4.2, D9.C, F5.1, PTCBP4.1
- new net N$45: F5.2, PTCBP4.2, R69.1
- new net N$46: D10.A, R70.2
- new net N$47: JP5.1, R70.1
- new net N$48: R57.1, R67.1, S5.2
- new net N$51: OSCMBP5.1, R72.2
- new net N$52: R74.2, R75.2, U12.1
- new net N$53: R76.1, VR6.1
- new net N$54: D11.C, D1BP5.2, F6.1, PTCBP5.1
- new net N$55: F6.2, PTCBP5.2, R83.1
- new net N$56: D12.A, R84.2
- new net N$57: JP6.1, R84.1
- new net N$58: R71.1, R81.1, S6.2
- new net OSCM4: OSCMBP4.2, R59.P$2, U9.11
- new net OSCM5: OSCMBP5.2, R73.P$2, U11.11
- new net OUT_A+4: J36.4, J37.4, U9.5
- new net OUT_A+5: J44.4, J45.4, U11.5
- new net OUT_A-4: J36.3, J37.3, U9.6
- new net OUT_A-5: J44.3, J45.3, U11.6
- new net OUT_B+4: J36.1, J37.1, U9.8
- new net OUT_B+5: J44.1, J45.1, U11.8
- new net OUT_B-4: J36.2, J37.2, U9.7
- new net OUT_B-5: J44.2, J45.2, U11.7
- new net RAW4: D1BP4.1, D9.A, J34.2, J35.VIN0, J38.2
- new net RAW5: D11.A, D1BP5.1, J42.2, J43.VIN0, J46.2
- new net VM4: C18.+, C19.1, R69.2, U10.3, U9.3
- new net VM5: C22.+, C23.1, R83.2, U11.3, U12.3
- new net VREF4: C20.1, J40.1, U9.10, VR5.2
- new net VREF5: C24.1, J48.1, U11.10, VR6.2
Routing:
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- added copper zone on layer 1, net GND4
- added copper zone on layer 15, net GND4
- added copper zone on layer 16, net GND4
- added copper zone on layer 2, net GND4
- added copper zone on layer 1, net GND5
- added copper zone on layer 15, net GND5
- added copper zone on layer 16, net GND5
- added copper zone on layer 2, net GND5
- added copper zone on layer 1, net N$44
- added copper zone on layer 1, net N$45
- added copper zone on layer 1, net N$54
- added copper zone on layer 1, net N$55
- added copper zone on layer 1, net OUT_A+4
- added copper zone on layer 1, net OUT_A+5
- added copper zone on layer 1, net OUT_A-4
- added copper zone on layer 1, net OUT_A-5
- added copper zone on layer 1, net OUT_B+4
- added copper zone on layer 1, net OUT_B+5
- added copper zone on layer 1, net OUT_B-4
- added copper zone on layer 1, net OUT_B-5
- added copper zone on layer 1, net VM4
- added copper zone on layer 1, net VM5
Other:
- board size 123.2 x 141.5 mm -> 122.2 x 192.5 mm
- board text added: "v10"
- board text removed: "Route Out"
- board text removed: "v01"
